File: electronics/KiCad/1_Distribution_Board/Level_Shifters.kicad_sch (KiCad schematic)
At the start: 24 parts, among them J24 Generic 2.54mm, J25 Generic 2.54mm, J26 Generic 2.54mm, J27 Generic 2.54mm, J28 Generic 2.54mm, J29 Generic 2.54mm, Q2 BS170, Q3 BS170

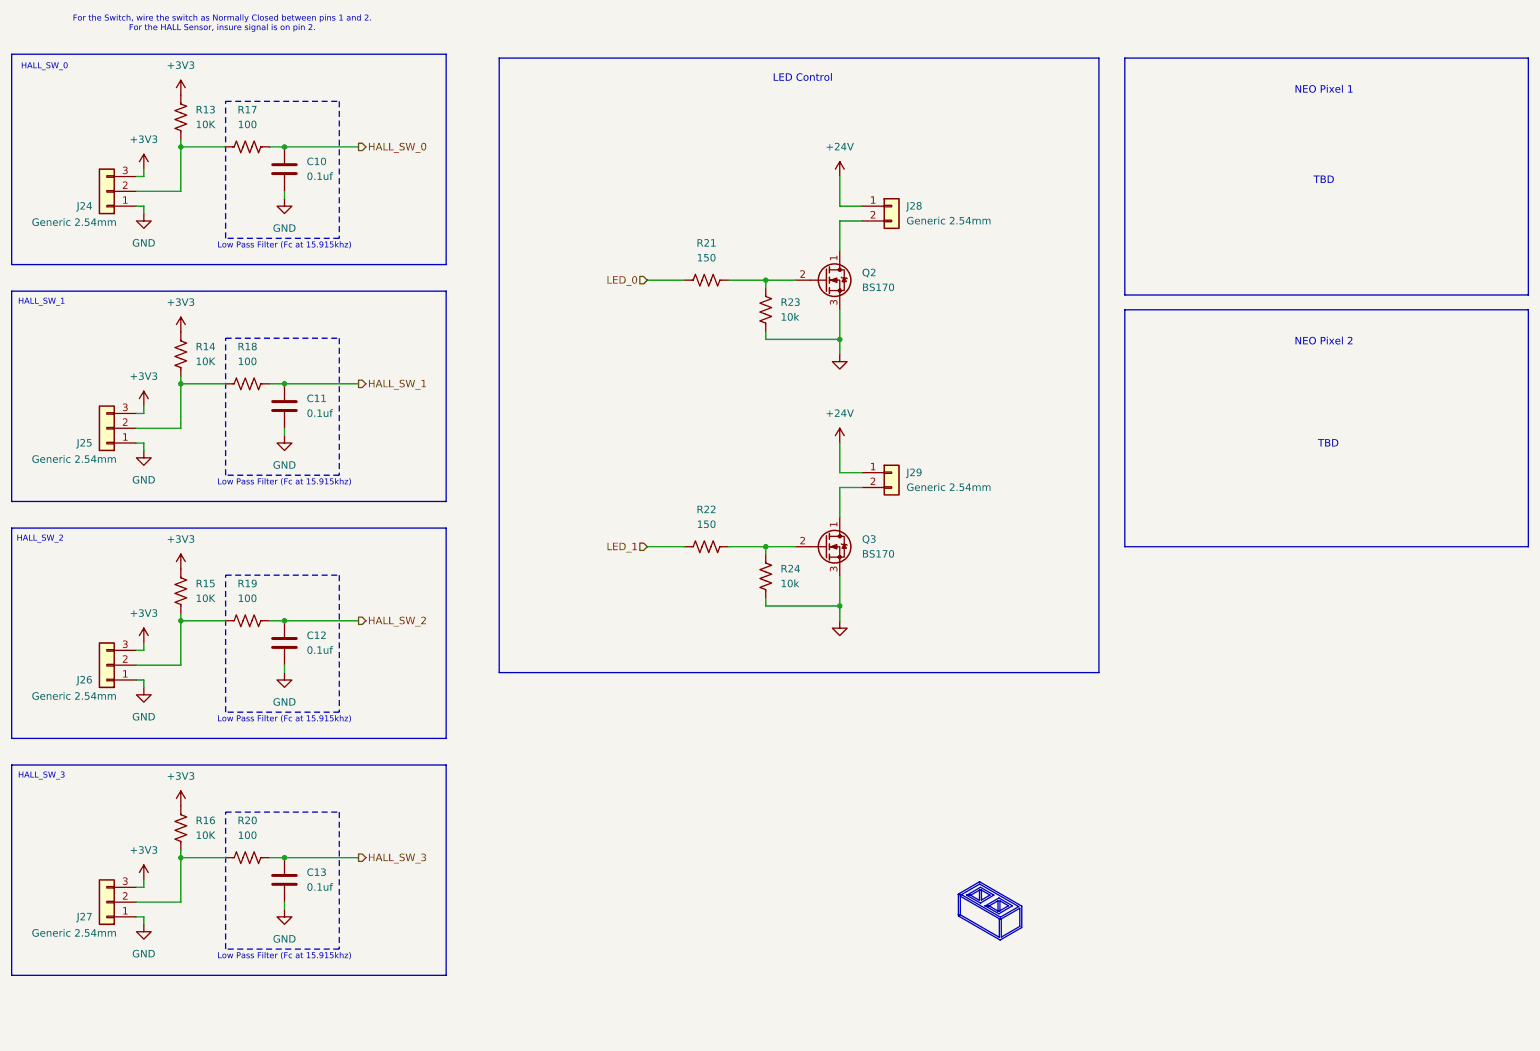
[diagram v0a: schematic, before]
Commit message: Merge board v1.3 into main (clean-clone fixups, generated files trimmed to main level) (#289)
* Initial start to updates

Removed motor pages, updated Q2,Q3, Cleaned up power module connections.

- Still need to correct routing for these updates.

* PCA Update

Updated PCA to have level shifter for I2C lines and external oscillator for precision. Corrected Power to pull from 12V.

* Removed old circuits from PCB

Removed all unused traces

* Mid work update

Lots of rework on the SCH and PCB. Checkpoint.

* Updated with more layout

Compelted PCA on board.

* adding libraries

* REV0.9 for review

Took care of all open items on the electronics PCB except for the driver resistor addresses.

* Updates Just prior to Ordering V1.0 PCBs

Updates Just prior to Ordering V1.0 PCBs

* Updates to push to V1.0

Updates to push to V1.0

* Updates to push to V1.0 missing saves. . .

Updates to push to V1.0 missing saves. . .

* Correcting Part rotation for JLCPCB

Several parts needed the "FT Rotation Offset" parameter added to correct for part orientation for JLCPCB order.

* All orientations corrected

* latest update

* Updated to reflect V1.0 of layer board as well

Updated for initial orders with PCA module populated. Also updated to layer boards for flex cables.

* Updated data and notes

* Corrected SCH for power sequence issue

5V to Vsys for all powered items.
Correction of the PCA9306 power pins.
Added decoupling to oscillator and PCA9306.

* Updated for changes to the SCH items

Updated PCB to include all changed from the SCH.

* Updated rules to correct errors

Cleaned up rules a bit to prevent false errors.

* Started work on silk update

Slowly started work on silk update.

* Corrected the 10k to 1k for connecting resistors

R1 got fixed for the correct 1k instead of 10k for UART1

* Updated Silk on PCB

Added notes for describing the pins better in the silk layer.

* Updated REV to 1.3 to reflect changes

* Updated with Version 1.3

* KiCad: make the v1.3 project 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
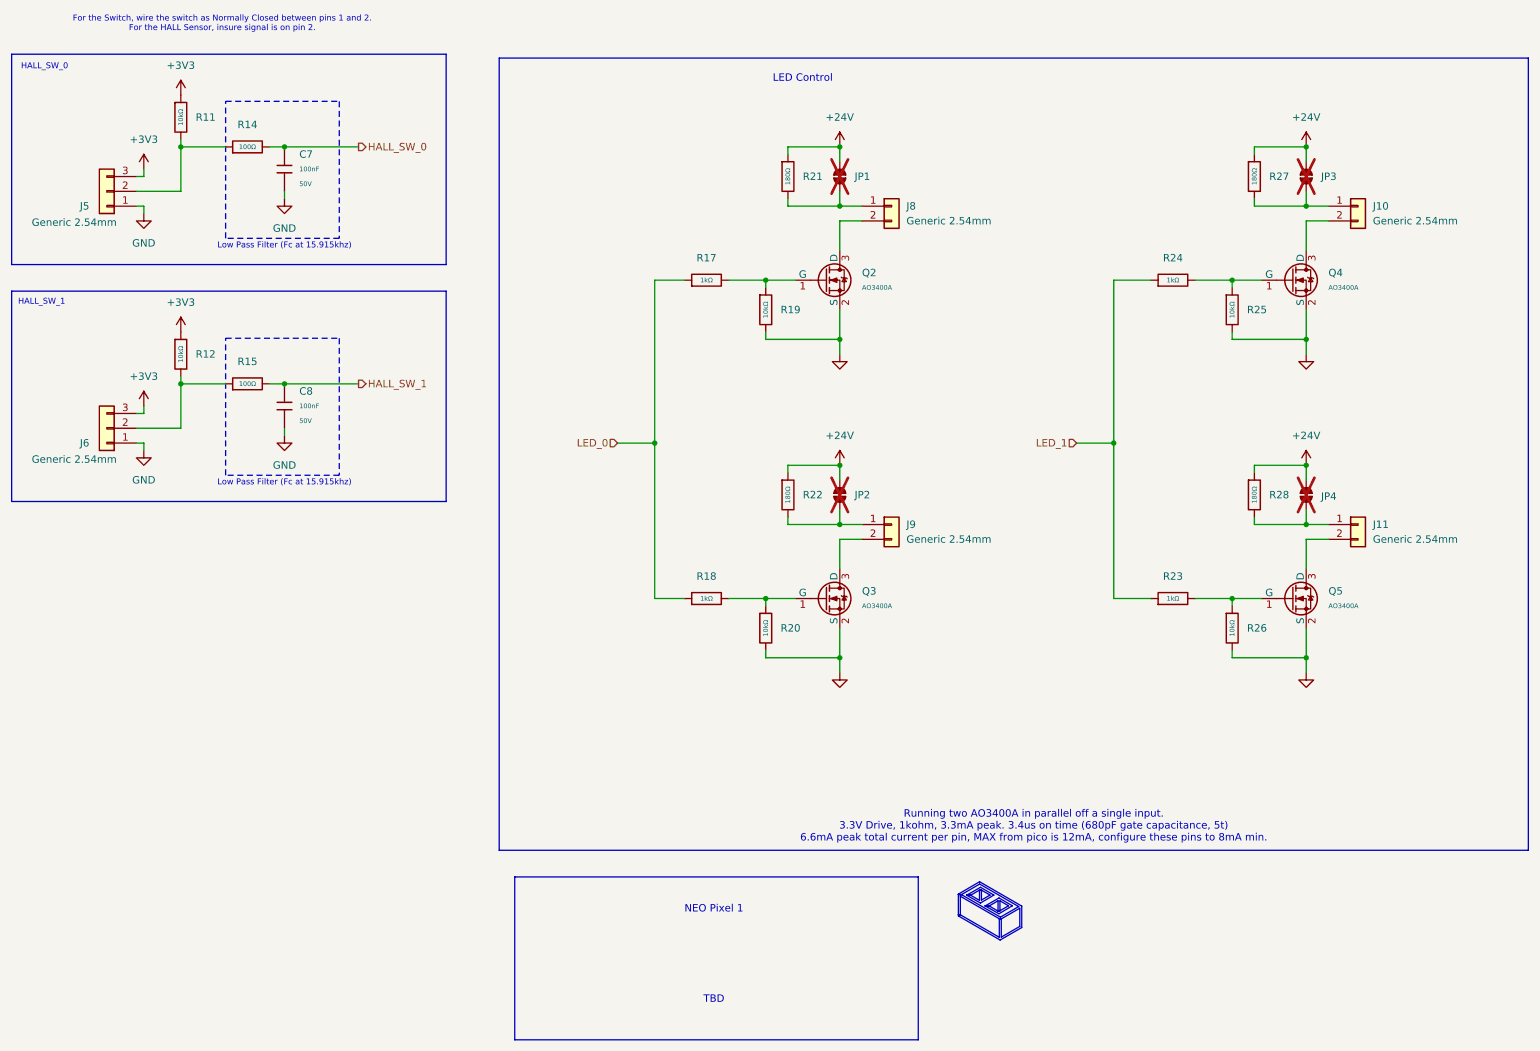
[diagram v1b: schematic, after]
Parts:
- removed C10, C11, C12, C13: 0.1uf, Capacitor_SMD:C_0805_2012Metric_Pad1.18x1.45mm_HandSolder, symbol Device:C
- removed J26, J27: Generic 2.54mm, Connector_PinHeader_2.54mm:PinHeader_1x03_P2.54mm_Vertical, symbol Connector_Generic:Conn_01x03
- removed Q2, Q3: BS170, Package_TO_SOT_THT:TO-92_Inline, symbol Transistor_FET:BS170
- removed R13, R14, R15, R16: 10K, Resistor_SMD:R_0805_2012Metric_Pad1.20x1.40mm_HandSolder, symbol Device:R_US
- removed R17, R18, R19, R20: 100, Resistor_SMD:R_0805_2012Metric_Pad1.20x1.40mm_HandSolder, symbol Device:R_US
- removed R21, R22: 150, Resistor_SMD:R_0805_2012Metric_Pad1.20x1.40mm_HandSolder, symbol Device:R_US
- removed R23, R24: 10k, Resistor_SMD:R_0805_2012Metric_Pad1.20x1.40mm_HandSolder, symbol Device:R_US
- added C7, C8: 100nF, PCM_JLCPCB:C_0603, symbol PCM_JLCPCB-Capacitors:0603,100nF
- added J10, J11: Generic 2.54mm, Connector_PinHeader_2.54mm:PinHeader_1x02_P2.54mm_Vertical, symbol Connector_Generic:Conn_01x02
- added JP1, JP2, JP3, JP4: ~, PCM_SparkFun-Jumper:Jumper_2_NO, symbol PCM_SparkFun-Jumper:SolderJumper_2_Open
- added Q2, Q3, Q4, Q5: AO3400A, PCM_JLCPCB:Q_SOT-23, symbol PCM_JLCPCB-Transistors:NMOS,AO3400A
- added R11, R12, R19, R20, R25, R26: 10kΩ, PCM_JLCPCB:R_0603, symbol PCM_JLCPCB-Resistors:0603,10kΩ
- added R14, R15: 100Ω, PCM_JLCPCB:R_0603, symbol PCM_JLCPCB-Resistors:0603,100Ω
- added R17, R18, R23, R24: 1kΩ, PCM_JLCPCB:R_0603, symbol PCM_JLCPCB-Resistors:0603,1kΩ
- added R21, R22, R27, R28: 180Ω, PCM_JLCPCB:R_1206, symbol PCM_JLCPCB-Resistors:1206,180Ω
- J5: renamed from J24; LCSC (none) -> C2937625
- J6: renamed from J25; LCSC (none) -> C2937625
- J8: renamed from J28; LCSC (none) -> C492401
- J9: renamed from J29; LCSC (none) -> C492401
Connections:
- net +24V: now also JP1.2 (B), JP2.2 (B), JP3.2 (B), JP4.2 (B), R21.1, R22.1, R27.1, R28.1; no longer J8.1 (Pin_1), J9.1 (Pin_1)
- net +3V3: now also R11.1, R12.1
- net GND: now also C7.2, C8.2, Q2.2 (S), Q3.2 (S), Q4.2 (S), Q5.2 (S), R19.2, R20.2, R25.2, R26.2
- net HALL_SW_0: now also C7.1, R14.2
- net HALL_SW_1: now also C8.1, R15.2
- net LED_0: now also R17.1, R18.1
- net LED_1: now also R23.1, R24.1
- net at J6.2 (Pin_2): now also R12.2, R15.1
- net at J5.2 (Pin_2): now also R11.2, R14.1
- net at J8.2 (Pin_2): now also Q2.3 (D)
- net at J9.2 (Pin_2): now also Q3.3 (D)
- new net: J8.1 (Pin_1), JP1.1 (A), R21.2
- new net: J11.1 (Pin_1), JP4.1 (A), R28.2
- new net: Q5.1 (G), R23.2, R26.1
- new net: Q3.1 (G), R18.2, R20.1
- new net: J10.1 (Pin_1), JP3.1 (A), R27.2
- new net: Q4.1 (G), R24.2, R25.1
- new net: J9.1 (Pin_1), JP2.1 (A), R22.2
- new net: J11.2 (Pin_2), Q5.3 (D)
- new net: Q2.1 (G), R17.2, R19.1
- new net: J10.2 (Pin_2), Q4.3 (D)
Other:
- note added: "Running two AO3400A in parallel off a single input. 3.3V Drive, 1kohm, 3.3mA peak. 3.4us on time (680pF gate capacitance, 5t) 6.6mA peak total current per pin, MAX from pico is 12mA, configure these pins to 8mA min."
- note removed: "HALL_SW_2"
- note removed: "HALL_SW_3"
- note removed: "NEO Pixel 2"
- moved on the sheet: J9
